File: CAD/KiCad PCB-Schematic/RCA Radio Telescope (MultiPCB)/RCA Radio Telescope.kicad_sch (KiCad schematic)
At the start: 11 parts, among them J1 5V In For Filter Board, J12 3V In For LNA, J2 9-12V From PoE Splitter, J3 3V Out For LNA, J4 5V Out For Filter Board, J5 Input from SDR, J6 USB_B_MICRO, U1 ZX60-P33ULN+, U2 ADALM Pluto SDR

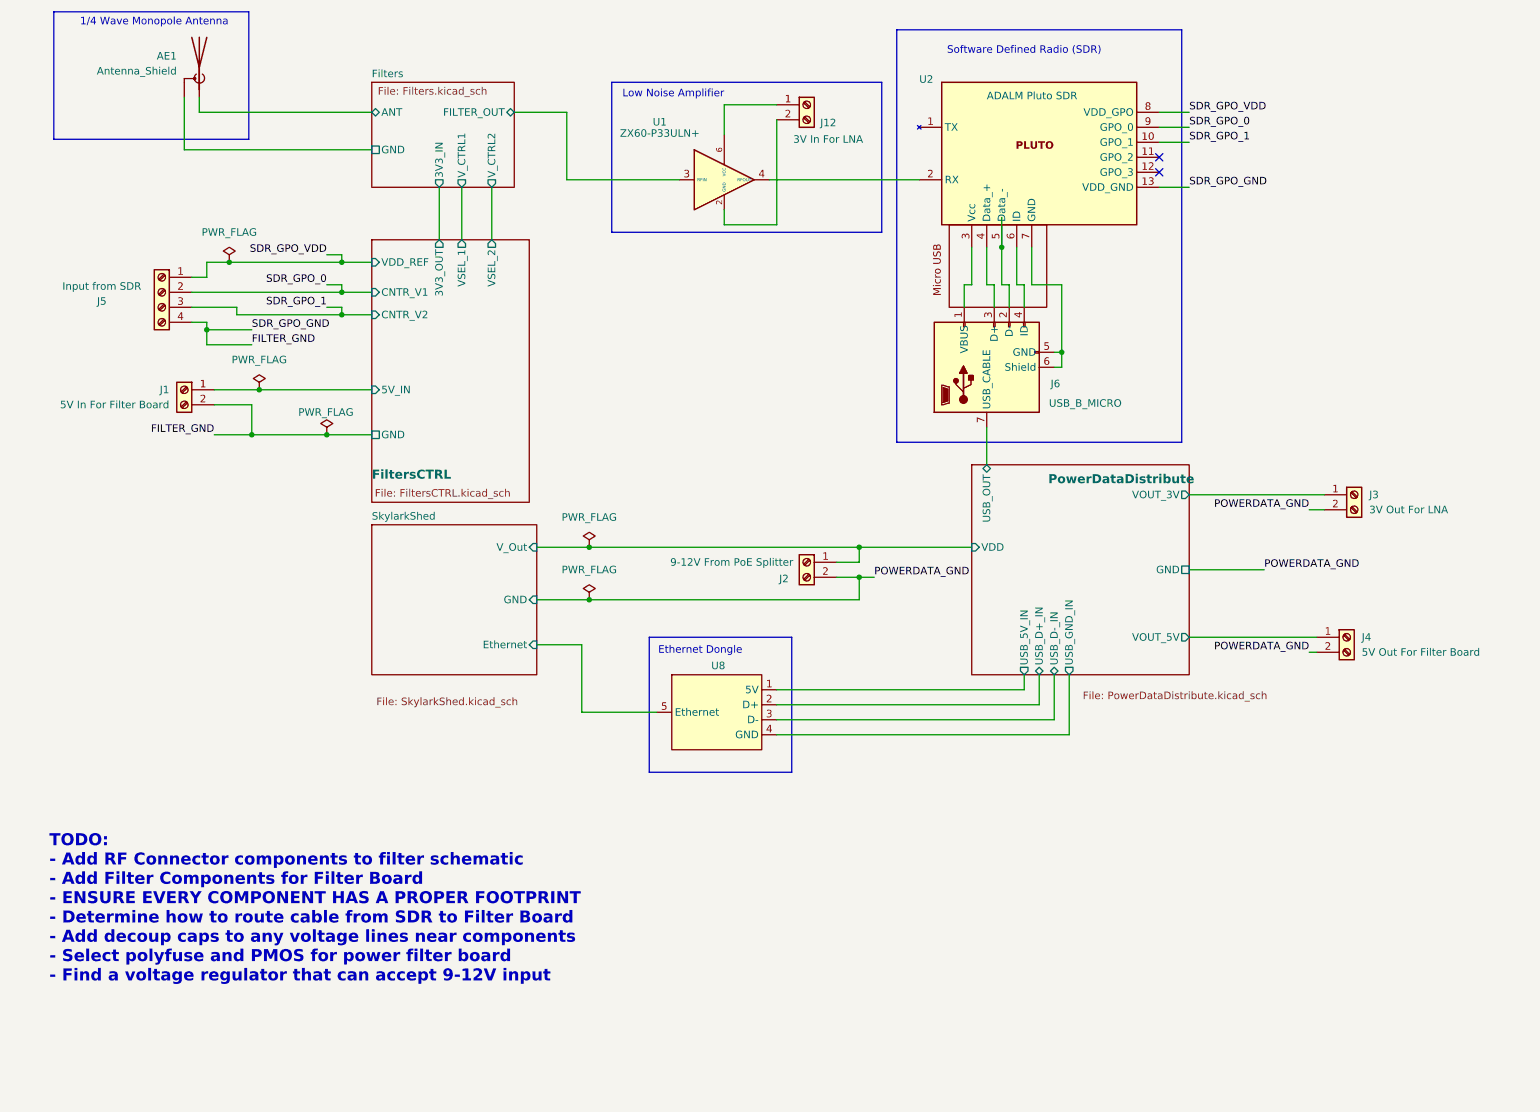
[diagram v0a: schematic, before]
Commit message: Update to Schematic and PCB
Filter Control Schematic to v1.5
- Removed redundant connector symbol

Root Schematic to v1.9
- Adjusted pin connections for J14 and J14

Created Matching Network PCB
- Filter Board Schematic renamed to MatchNetwork
- Placed RF switches, traces, holes for daughter board, and ground stitching
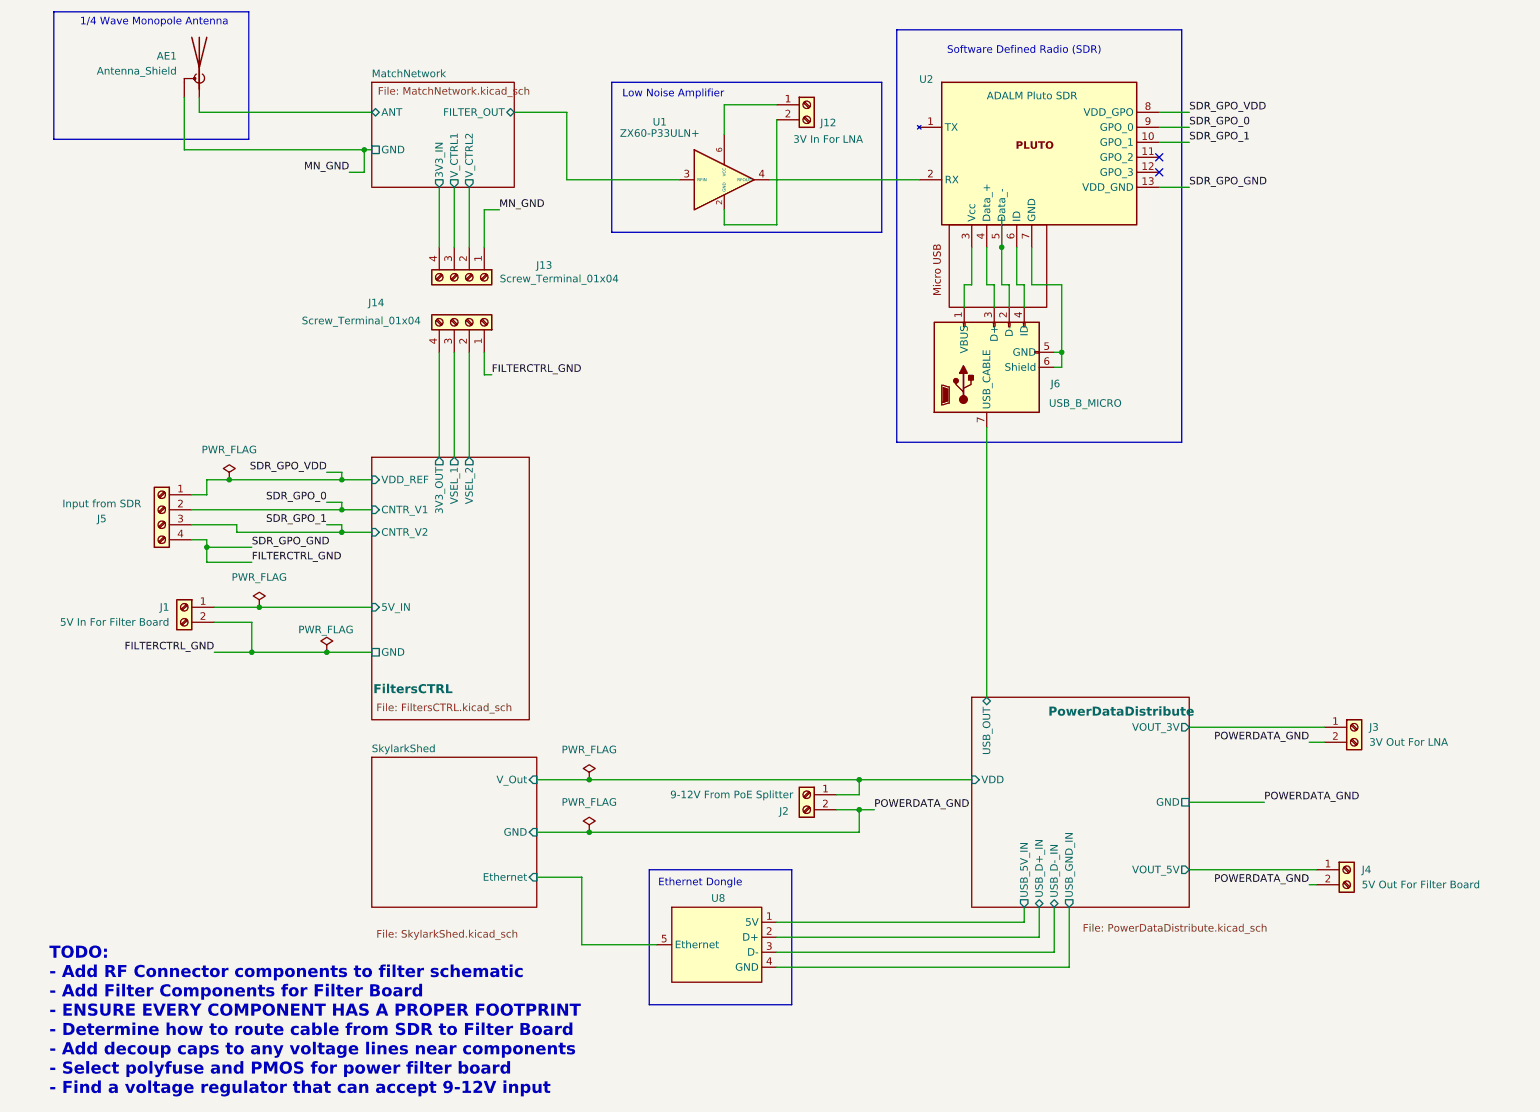
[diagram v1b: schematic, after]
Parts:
- added J13, J14: Screw_Terminal_01x04, Connector_PinHeader_2.54mm:PinHeader_1x04_P2.54mm_Vertical, symbol Connector:Screw_Terminal_01x04
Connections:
- net MatchNetwork/3V3_IN: now also J13.4 (Pin_4)
- net MatchNetwork/V_CTRL1: now also J13.3 (Pin_3)
- net MatchNetwork/V_CTRL2: now also J13.2 (Pin_2)
- net FILTER_GND renamed FILTERCTRL_GND
- net FILTERCTRL_GND: now also J14.1 (Pin_1)
- net MatchNetwork/GND renamed MN_GND
- net MN_GND: now also J13.1 (Pin_1)
- new net FiltersCTRL/3V3_OUT: J14.4 (Pin_4)
- new net FiltersCTRL/VSEL_1: J14.3 (Pin_3)
- new net FiltersCTRL/VSEL_2: J14.2 (Pin_2)
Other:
- sheet Filters renamed MatchNetwork
- sheet MatchNetwork: file Filters.kicad_sch -> MatchNetwork.kicad_sch
- moved on the sheet: J1, J2, J3, J4, J5, U8

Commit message: Updated Schematics and PCBs
Root Schematic to v2.0
- Swapped Matching Network segment for SMD filter
- Updated TODO list

SMD Filter PCB to v1.0
- Added filter and SMA connector footprints
- Imported ADS trace layout
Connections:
- net MN_GND: no longer AE1.2 (Shield)
- net MatchNetwork/ANT: no longer AE1.1 (A)
- net MatchNetwork/FILTER_OUT: no longer U1.3 (RFIN)
- new net SMDFilter/GND: AE1.2 (Shield)
- new net SMDFilter/SIGNAL_IN: AE1.1 (A)
- new net SMDFilter/SIGNAL_OUT: U1.3 (RFIN)
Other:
- added sheet SMDFilter (SMDFilter.kicad_sch)
- note added: "Extra Designs"
- note added: "TODO: - Fix ERC Problems"
- note removed: "TODO: - Add RF Connector components to filter schematic - Add Filter Components for Filter Board - ENSURE EVERY COMPONENT HAS A PROPER FOOTPRINT - Determine how to route cable from SDR to Filter Board - Add decoup caps to any voltage lines near components - Select polyfuse and PMOS for power filter board - Find a voltage regulator that can accept 9-12V input"
- moved on the sheet: J1, J13, J14, J2, J3, J4, J5, U8

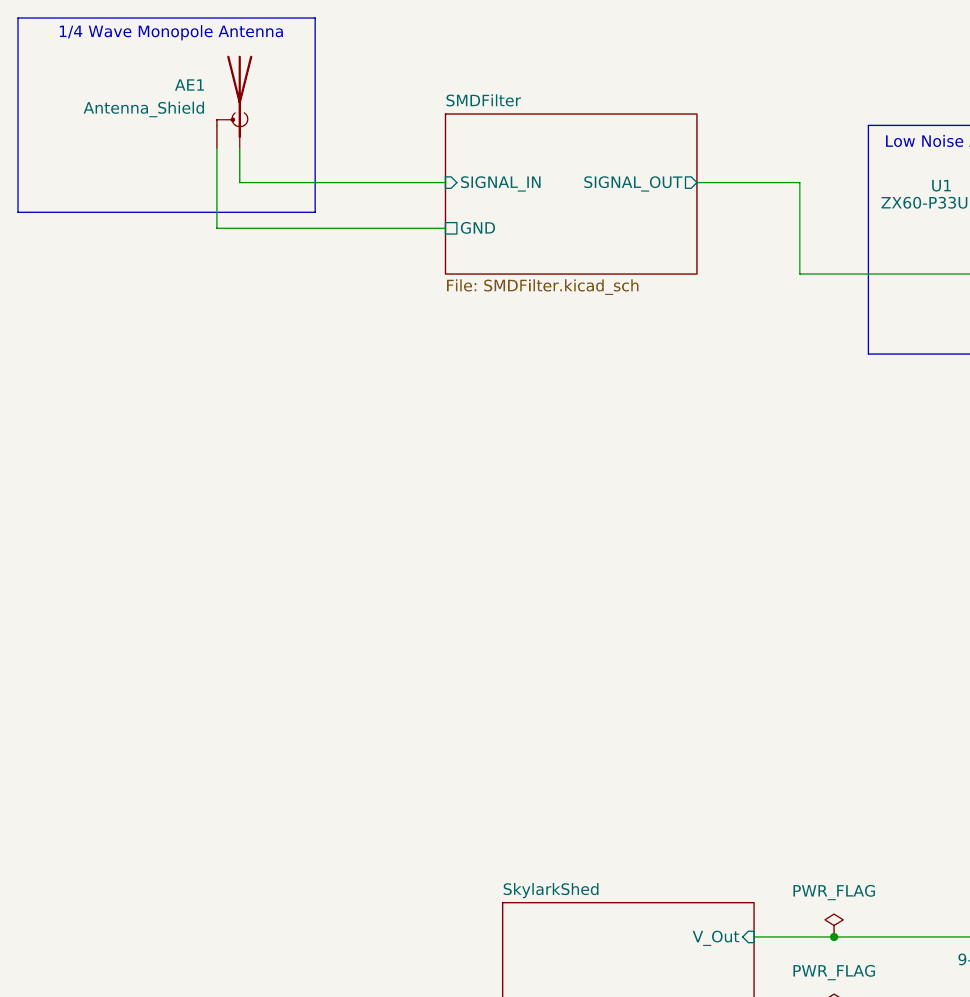
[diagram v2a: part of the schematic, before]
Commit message: Add 1.6 GHZ Matching Network PCB v1.0
- Same design as original board, but with 1.6 GHz matching network
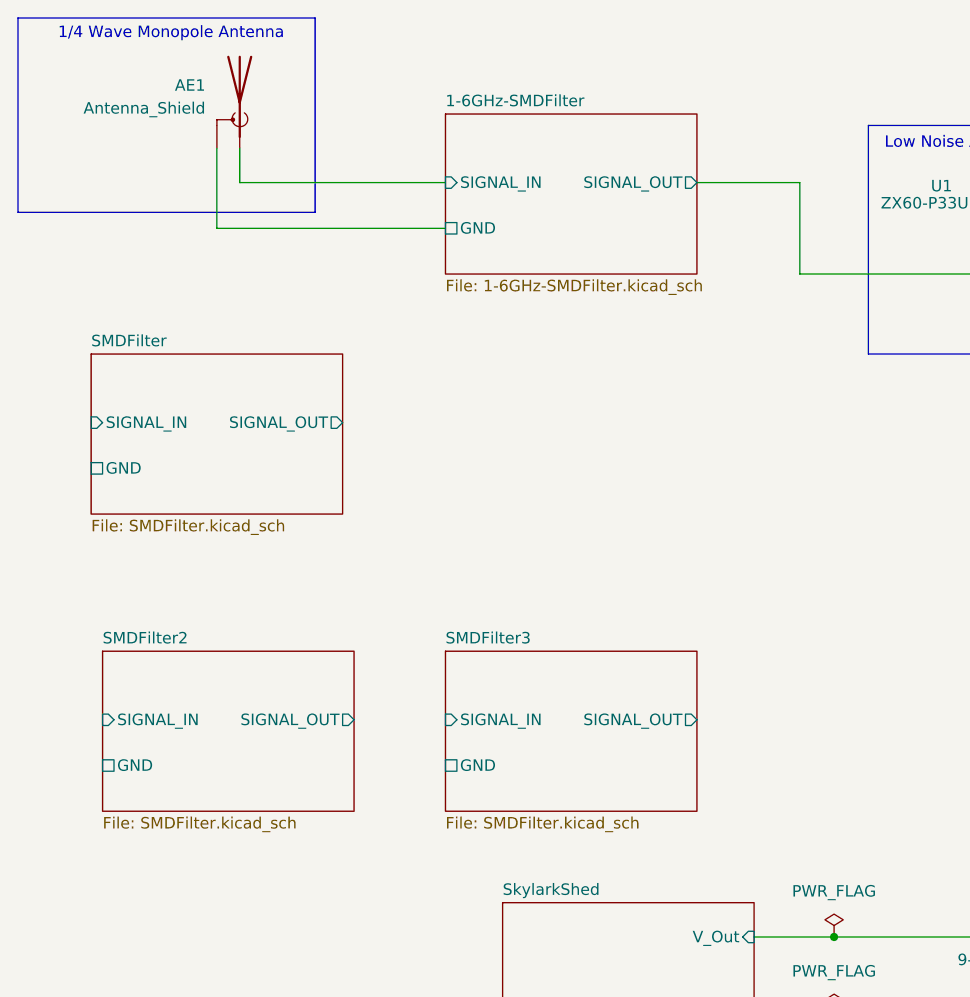
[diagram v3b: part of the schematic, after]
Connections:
- net SMDFilter/GND: no longer AE1.2 (Shield)
- net SMDFilter/SIGNAL_IN: no longer AE1.1 (A)
- net SMDFilter/SIGNAL_OUT: no longer U1.3 (RFIN)
- new net 1-6GHz-SMDFilter/GND: AE1.2 (Shield)
- new net 1-6GHz-SMDFilter/SIGNAL_IN: AE1.1 (A)
- new net 1-6GHz-SMDFilter/SIGNAL_OUT: U1.3 (RFIN)
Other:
- added sheet 1-6GHz-SMDFilter (1-6GHz-SMDFilter.kicad_sch)
- added sheet SMDFilter2 (SMDFilter.kicad_sch)
- added sheet SMDFilter3 (SMDFilter.kicad_sch)

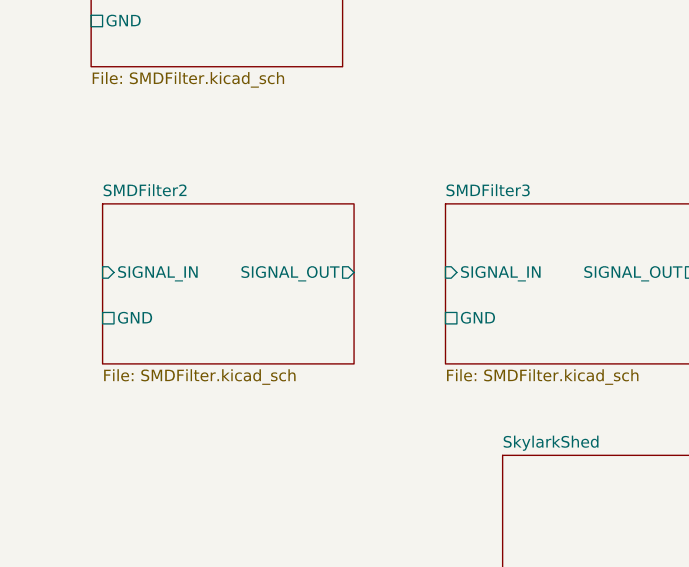
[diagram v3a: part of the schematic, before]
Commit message: Added Coupled Lines Filter PCB v1.0 and Exported PD Board Step File
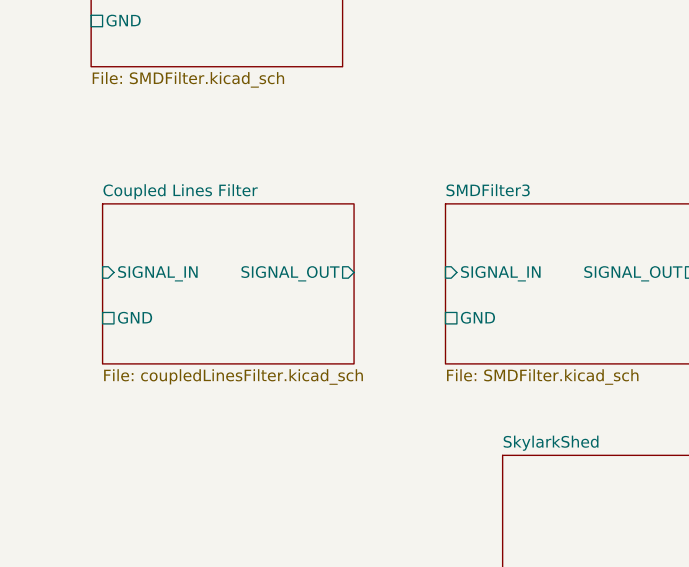
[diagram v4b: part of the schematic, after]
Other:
- sheet SMDFilter2 renamed Coupled Lines Filter
- sheet Coupled Lines Filter: file SMDFilter.kicad_sch -> coupledLinesFilter.kicad_sch
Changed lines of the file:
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@@
 			(color 0 0 0 0.0000)
 		)
-		(property "Sheetname" "SMDFilter2"
+		(property "Sheetname" "Coupled Lines Filter"
 			(at 26.67 86.9184 0)
 			(effects
@@
 			)
 		)
-		(property "Sheetfile" "SMDFilter.kicad_sch"
+		(property "Sheetfile" "coupledLinesFilter.kicad_sch"
 			(at 26.67 105.9946 0)
 			(effects

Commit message: RF Boards Redo (WIP)
- Overhauling current RF boards to keep 4 RF boards in total
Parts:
- removed J1: 5V In For Filter Board, Library:CONN_1729128_PXC, symbol Connector:Screw_Terminal_01x02
- removed J13, J14: Screw_Terminal_01x04, Connector_PinHeader_2.54mm:PinHeader_1x04_P2.54mm_Vertical, symbol Connector:Screw_Terminal_01x04
- removed J5: Input from SDR, Library:PHOENIX_1729144, symbol Connector:Screw_Terminal_01x04
- added J1: Screw_Terminal_01x04, Library:PHOENIX_1729144, symbol Connector:Screw_Terminal_01x04
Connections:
- net MN_GND: now also J1.1 (Pin_1)
- net FILTERCTRL_GND renamed SDR_GPO_GND
- new net RFSwitchFilter/CNTR_V1: J1.3 (Pin_3)
- new net RFSwitchFilter/CNTR_V2: J1.2 (Pin_2)
- new net RFSwitchFilter/VDD_REF: J1.4 (Pin_4)
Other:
- sheet 1-6GHz-SMDFilter renamed Matched Distributive Filter
- sheet Coupled Lines Filter renamed Matched SMD Filter
- removed sheet FiltersCTRL
- removed sheet MatchNetwork
- removed sheet SMDFilter3
- added sheet RFSwitchFilter (rfswitchFilter.kicad_sch)
- sheet Matched Distributive Filter: file 1-6GHz-SMDFilter.kicad_sch -> RF Boards/matchedDistributeFilter.kicad_sch
- sheet Matched SMD Filter: file coupledLinesFilter.kicad_sch -> RF Boards/matchedSMDFilter.kicad_sch
- sheet SMDFilter: file SMDFilter.kicad_sch -> RF Boards/SMDFilter.kicad_sch
- note added: "TODO: - Fix ERC Problems - Add 5V Source from SDR"
- note removed: "Extra Designs"
- note removed: "TODO: - Fix ERC Problems"
